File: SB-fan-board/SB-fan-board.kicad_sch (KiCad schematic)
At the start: 15 parts, among them J1 FAN0, J2 FAN1, J3 NEO, J4 MAIN, U1 TPS54302

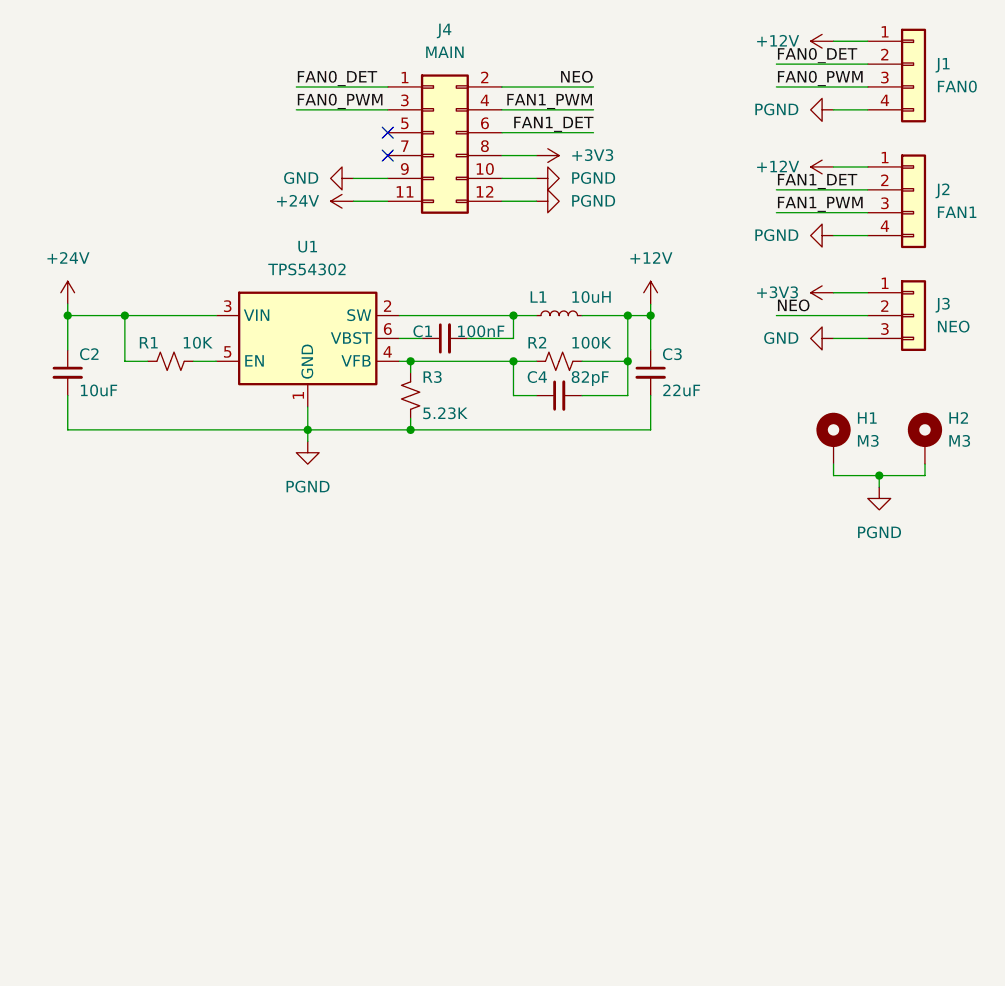
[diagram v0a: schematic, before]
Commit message: update fan board to v2
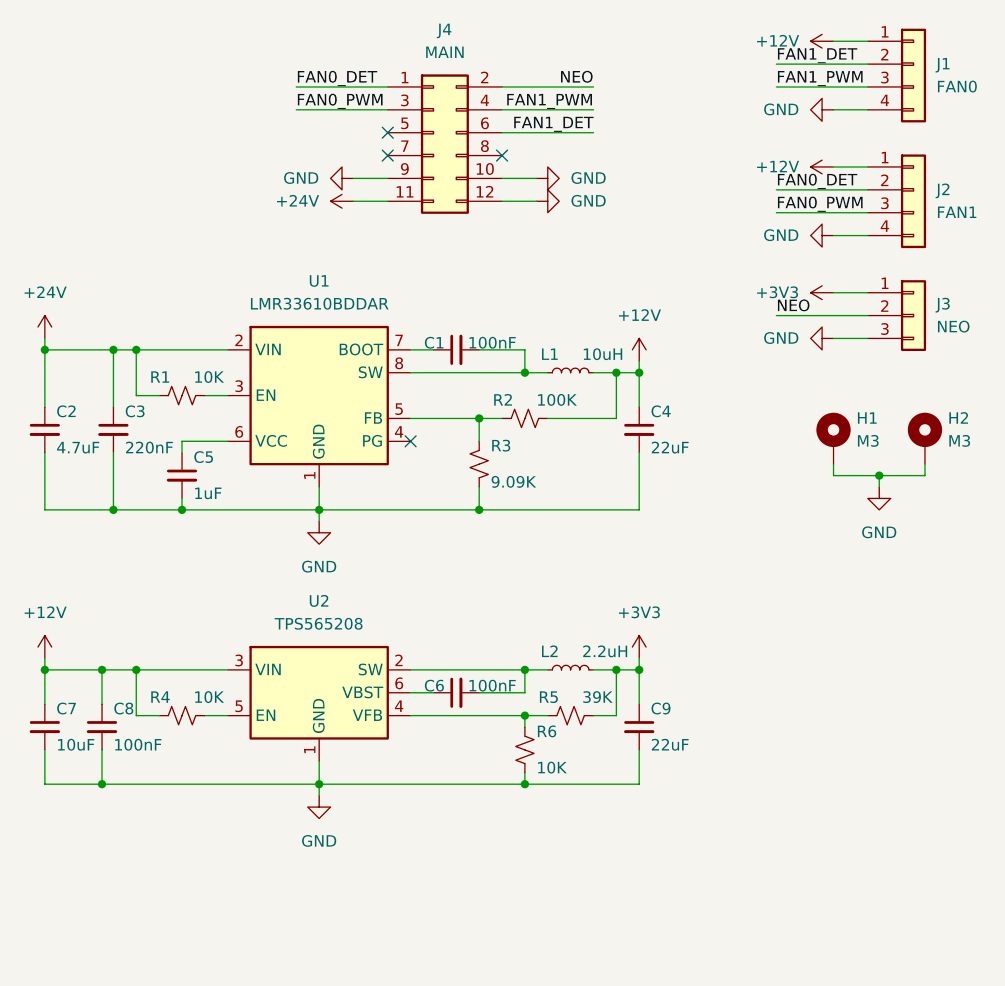
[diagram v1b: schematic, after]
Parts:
- removed C4: 82pF, Capacitor_SMD:C_0603_1608Metric, symbol Device:C_Small
- removed U1: TPS54302, Package_TO_SOT_SMD:SOT-23-6, symbol Regulator_Switching:TPS565208
- added C3: 220nF, Capacitor_SMD:C_0603_1608Metric, symbol Device:C_Small
- added C5: 1uF, Capacitor_SMD:C_0603_1608Metric, symbol Device:C_Small
- added C6, C8: 100nF, Capacitor_SMD:C_0603_1608Metric, symbol Device:C_Small
- added C7: 10uF, Capacitor_SMD:C_0805_2012Metric, symbol Device:C_Small
- added C9: 22uF, Capacitor_SMD:C_0805_2012Metric, symbol Device:C_Small
- added L2: 2.2uH, Inductor_SMD:L_Murata_DFE201610P, symbol Device:L_Small
- added R4, R6: 10K, Resistor_SMD:R_0603_1608Metric, symbol Device:R_Small_US
- added R5: 39K, Resistor_SMD:R_0603_1608Metric, symbol Device:R_Small_US
- added U1: LMR33610BDDAR, Package_SO:Texas_HSOP-8-1EP_3.9x4.9mm_P1.27mm, symbol Regulator_Switching:LMR33610BDDAR
- added U2: TPS565208, Package_TO_SOT_SMD:SOT-23-6, symbol Regulator_Switching:TPS565208
- C2: value 10uF -> 4.7uF
- R3: value 5.23K -> 9.09K
- renumbered C3 to C4
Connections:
- net PGND is gone; now on net GND: C2.2, C4.2, H1.1, H2.1, J1.4 (Pin_4), J2.4 (Pin_4), J4.10 (Pin_10), J4.12 (Pin_12), R3.2
- net +12V: now also C7.1, C8.1, R4.1, U2.3 (VIN)
- net +24V: now also C3.1, U1.2 (VIN)
- net +3V3: now also C9.1, L2.2, R5.2; no longer J4.8 (Pin_8)
- net FAN0_DET: now also J2.2 (Pin_2); no longer J1.2 (Pin_2)
- net FAN0_PWM: now also J2.3 (Pin_3); no longer J1.3 (Pin_3)
- net FAN1_DET: now also J1.2 (Pin_2); no longer J2.2 (Pin_2)
- net FAN1_PWM: now also J1.3 (Pin_3); no longer J2.3 (Pin_3)
- net GND: now also C3.2, C5.2, C7.2, C8.2, C9.2, R6.2, U1.1 (GND), U1.9 (GND), U2.1 (GND)
- net at C1.1: now also U1.7 (BOOT)
- net at C1.2, L1.1: now also U1.8 (SW)
- net at R2.1, R3.1: now also U1.5 (FB)
- net at R1.2: now also U1.3 (EN)
- new net: C5.1, U1.6 (VCC)
- new net: C6.2, L2.1, U2.2 (SW)
- new net: R5.1, R6.1, U2.4 (VFB)
- new net: R4.2, U2.5 (EN)
- new net: C6.1, U2.6 (VBST)
- no-connect marks 2 -> 4
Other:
- moved on the sheet: C1, C2, C4, L1, R1, R2, R3

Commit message: generate manufacture files
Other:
- company: (none) -> Lassi-Cat
- title: (none) -> StealthBurner CAN Fan
- moved on the sheet: C1, C2, C3, C4, C5, C6, C7, C8, C9, L1, L2, R1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

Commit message: footprint: change input cap to 1206
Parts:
- C2: footprint Capacitor_SMD:C_0805_2012Metric -> Capacitor_SMD:C_1206_3216Metric
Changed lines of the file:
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@@
 			)
 		)
-		(property "Footprint" "Capacitor_SMD:C_0805_2012Metric"
+		(property "Footprint" "Capacitor_SMD:C_1206_3216Metric"
 			(at 31.75 139.7 0)
 			(effects

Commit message: misc: update to kicad 9
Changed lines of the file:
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@@
 (kicad_sch
-	(version 20231120)
+	(version 20250114)
 	(generator "eeschema")
-	(generator_version "8.0")
+	(generator_version "9.0")
 	(paper "A4")
 	(title_block
@@
 	(label "FAN1_PWM"
 		(at 92.71 91.44 180)
-		(fields_autoplaced yes)
 		(effects
 			(font
@@
 	(label "FAN1_DET"
 		(at 113.03 86.36 0)
-		(fields_autoplaced yes)
 		(effects
 			(font
@@
 	(label "FAN0_PWM"
 		(at 113.03 102.87 0)
-		(fields_autoplaced yes)
 		(effects
 			(font
@@
 	(label "FAN0_PWM"
 		(at 59.69 91.44 0)
-		(fields_autoplaced yes)
 		(effects
 			(font
@@
 	(label "NEO"
 		(at 92.71 88.9 180)
-		(fields_autoplaced yes)
 		(effects
 			(font
@@
 	(label "FAN1_PWM"
 		(at 113.03 88.9 0)
-		(fields_autoplaced yes)
 		(effects
 			(font
@@
 	(label "FAN1_DET"
 		(at 92.71 93.98 180)
-		(fields_autoplaced yes)
 		(effects
 			(font
@@
 	(label "FAN0_DET"
 		(at 113.03 100.33 0)
-		(fields_autoplaced yes)
 		(effects
 			(font
@@
 	(label "NEO"
 		(at 113.03 114.3 0)
-		(fields_autoplaced yes)
 		(effects
 			(font
@@
 	(label "FAN0_DET"
 		(at 59.69 88.9 0)
-		(fields_autoplaced yes)
 		(effects
 			(font
@@
 		)
 	)
+	(embedded_fonts no)
 )
